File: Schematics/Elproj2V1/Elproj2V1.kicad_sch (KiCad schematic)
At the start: 16 parts, among them J1 Conn_01x04_Pin, Q1 PMOS, Q2 NMOS, SW2 Manual

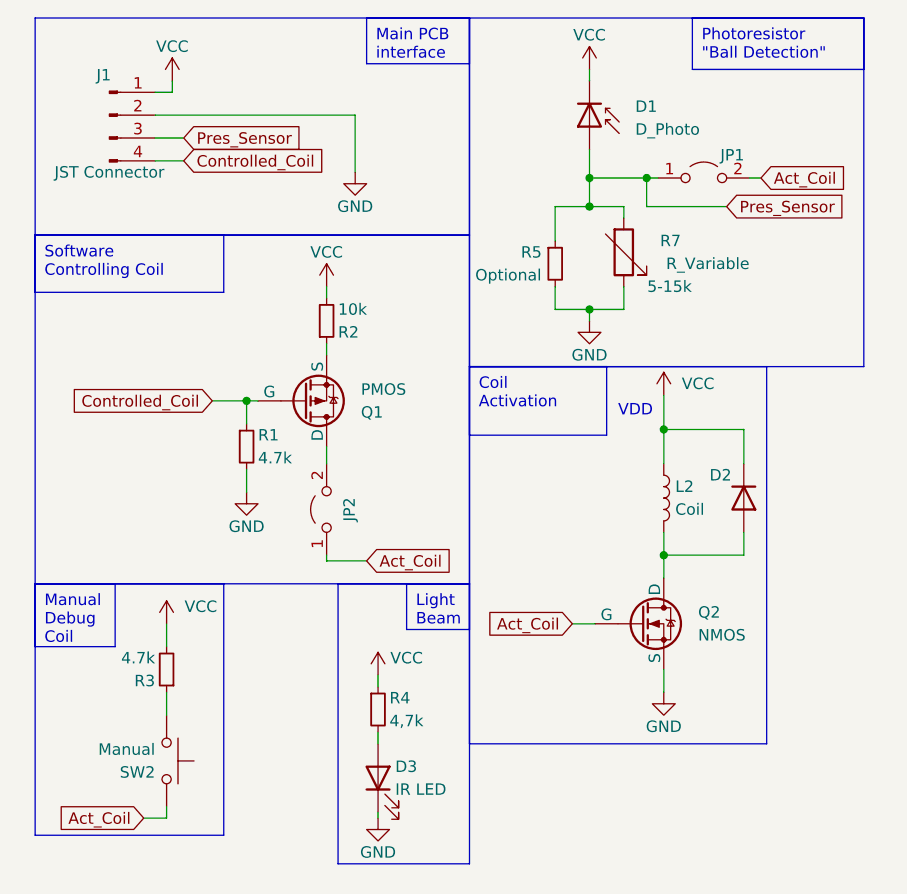
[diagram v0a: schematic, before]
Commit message: ReOrganizing Structure
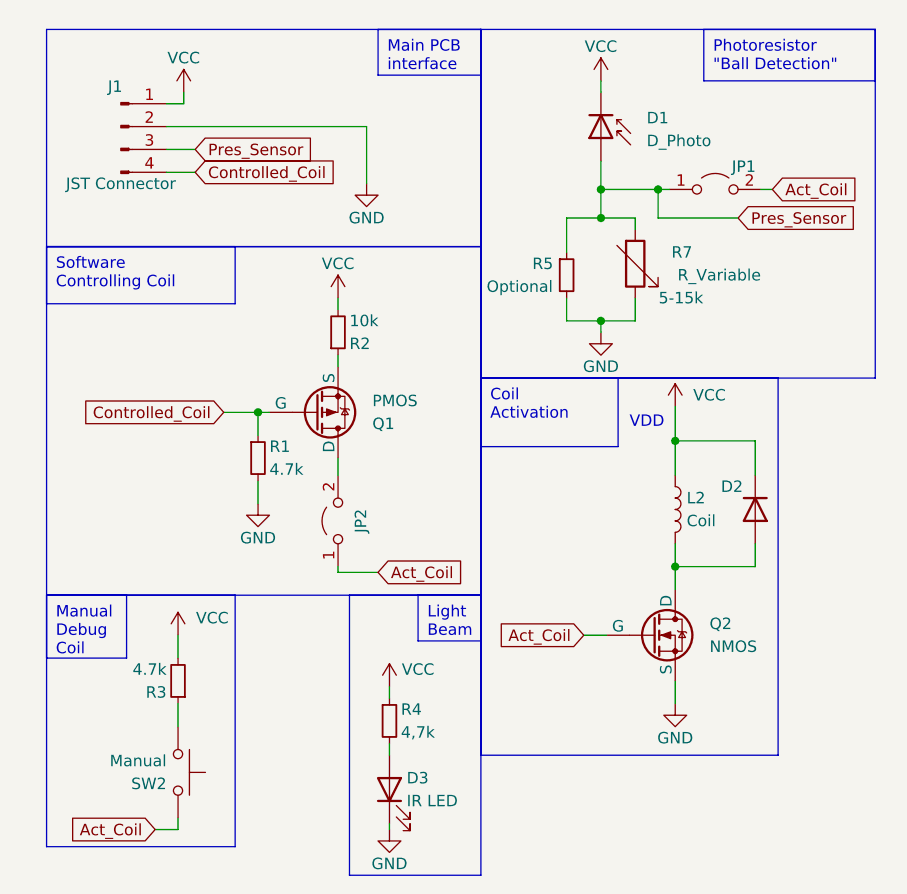
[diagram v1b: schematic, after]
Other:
- moved on the sheet: D1, D2, D3, J1, JP1, JP2, L2, Q1, Q2, R1, R2, R3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
